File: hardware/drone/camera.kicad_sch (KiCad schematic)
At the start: 15 parts, among them J1 54548-2272, U1 STM32N645I0, U21 TCA9406DC, U25 ECMF2-40100N6, U26 ECMF2-40100N6, U27 ECMF2-40100N6

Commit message: Started footprint assignments
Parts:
- D6, D7, D8, D9: footprint Package_DIP:DIP-40_W15.24mm -> (none)
- U25, U26, U27: footprint Package_DFN_QFN:ST_UQFN-6L_1.5x1.7mm_P0.5mm -> (none)
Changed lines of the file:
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@@
 			)
 		)
-		(property "Footprint" "Package_DFN_QFN:ST_UQFN-6L_1.5x1.7mm_P0.5mm"
+		(property "Footprint" ""
 			(at 146.05 27.94 0)
 			(hide yes)
@@
 			)
 		)
-		(property "Footprint" "Package_DFN_QFN:ST_UQFN-6L_1.5x1.7mm_P0.5mm"
+		(property "Footprint" ""
 			(at 146.05 44.45 0)
 			(hide yes)
@@
 			)
 		)
-		(property "Footprint" "Package_DIP:DIP-40_W15.24mm"
+		(property "Footprint" ""
 			(at 234.95 121.92 0)
 			(hide yes)
@@
 			)
 		)
-		(property "Footprint" "Package_DFN_QFN:ST_UQFN-6L_1.5x1.7mm_P0.5mm"
+		(property "Footprint" ""
 			(at 146.05 60.96 0)
 			(hide yes)
@@
 			)
 		)
-		(property "Footprint" "Package_DIP:DIP-40_W15.24mm"
+		(property "Footprint" ""
 			(at 207.01 121.92 0)
 			(hide yes)
@@
 			)
 		)
-		(property "Footprint" "Package_DIP:DIP-40_W15.24mm"
+		(property "Footprint" ""
 			(at 220.98 121.92 0)
 			(hide yes)
@@
 			)
 		)
-		(property "Footprint" "Package_DIP:DIP-40_W15.24mm"
+		(property "Footprint" ""
 			(at 248.92 121.92 0)
 			(hide yes)

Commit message: Continued footprint assignments
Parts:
- U21: footprint (none) -> Package_SO:VSSOP-8_2.3x2mm_P0.5mm
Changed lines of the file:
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@@
 			)
 		)
-		(property "Footprint" ""
+		(property "Footprint" "Package_SO:VSSOP-8_2.3x2mm_P0.5mm"
 			(at 62.23 129.54 0)
 			(hide yes)

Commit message: More footprints
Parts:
- removed U25, U26, U27: ECMF2-40100N6, symbol SoftDrone:ECMF2-40100N6
- added U25, U26, U27: ECMF2-40A100N6, ECMF2-40A100N6:ECMF240A100N6, symbol SoftDrone:ECMF2-40A100N6
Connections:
- net CSI_CKN: now also U25.6 (D+_ic)
- net CSI_CKN_CON: now also U25.1 (D+_con)
- net CSI_CKP: now also U25.5 (D-_ic)
- net CSI_CKP_CON: now also U25.2 (D-_con)
- net CSI_D0N: now also U26.6 (D+_ic)
- net CSI_D0N_CON: now also U26.1 (D+_con)
- net CSI_D0P: now also U26.5 (D-_ic)
- net CSI_D0P_CON: now also U26.2 (D-_con)
- net CSI_D1N: now also U27.6 (D+_ic)
- net CSI_D1N_CON: now also U27.1 (D+_con)
- net CSI_D1P: now also U27.5 (D-_ic)
- net CSI_D1P_CON: now also U27.2 (D-_con)
- net GND: now also U25.3 (GND), U25.4 (GND), U26.3 (GND), U26.4 (GND), U27.3 (GND), U27.4 (GND)

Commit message: More footprints
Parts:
- C116, C117: footprint (none) -> Capacitor_SMD:C_0402_1005Metric
- D6, D7, D8, D9: footprint (none) -> SoftDroneLibrary:TPD1E1B04DPYR
- R34: footprint (none) -> Resistor_SMD:R_0402_1005Metric
- R41, R42: footprint (none) -> Resistor_SMD:R_0603_1608Metric
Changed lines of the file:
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@@
 			)
 		)
-		(property "Footprint" ""
+		(property "Footprint" "SoftDroneLibrary:TPD1E1B04DPYR"
 			(at 234.95 121.92 0)
 			(hide yes)
@@
 			)
 		)
-		(property "Footprint" ""
+		(property "Footprint" "Resistor_SMD:R_0603_1608Metric"
 			(at 150.622 114.3 90)
 			(hide yes)
@@
 			)
 		)
-		(property "Footprint" ""
+		(property "Footprint" "Resistor_SMD:R_0402_1005Metric"
 			(at 78.74 72.898 90)
 			(hide yes)
@@
 			)
 		)
-		(property "Footprint" ""
+		(property "Footprint" "SoftDroneLibrary:TPD1E1B04DPYR"
 			(at 207.01 121.92 0)
 			(hide yes)
@@
 			)
 		)
-		(property "Footprint" ""
+		(property "Footprint" "Capacitor_SMD:C_0402_1005Metric"
 			(at 85.3948 121.92 0)
 			(hide yes)
@@
 			)
 		)
-		(property "Footprint" ""
+		(property "Footprint" "Resistor_SMD:R_0603_1608Metric"
 			(at 141.732 114.3 90)
 			(hide yes)
@@
 			)
 		)
-		(property "Footprint" ""
+		(property "Footprint" "SoftDroneLibrary:TPD1E1B04DPYR"
 			(at 220.98 121.92 0)
 			(hide yes)
@@
 			)
 		)
-		(property "Footprint" ""
+		(property "Footprint" "Capacitor_SMD:C_0402_1005Metric"
 			(at 59.3852 121.92 0)
 			(hide yes)
@@
 			)
 		)
-		(property "Footprint" ""
+		(property "Footprint" "SoftDroneLibrary:TPD1E1B04DPYR"
 			(at 248.92 121.92 0)
 			(hide yes)

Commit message: Labeled nets, added colours, and fixed stm32n6 schematic symbol issues
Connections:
- net CSI_REXT: now reaches R34.1, U1.N5 (CSI_REXT)
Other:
- moved on the sheet: R34
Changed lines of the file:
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@@
+	(wire
+		(pts
+			(xy 71.12 71.12) (xy 78.74 71.12)
+		)
+		(stroke
+			(width 0)
+			(type default)
+		)
+	)
 	(wire
 		(pts
@@
 	(wire
 		(pts
-			(xy 86.36 71.12) (xy 86.36 73.66)
+			(xy 90.17 71.12) (xy 90.17 73.66)
 		)
 		(stroke
@@
 	(wire
 		(pts
-			(xy 82.55 71.12) (xy 86.36 71.12)
+			(xy 86.36 71.12) (xy 90.17 71.12)
 		)
 		(stroke
@@
 	(wire
 		(pts
-			(xy 71.12 71.12) (xy 74.93 71.12)
-		)
-		(stroke
-			(width 0)
-			(type default)
-		)
-	)
-	(wire
-		(pts
 			(xy 172.72 113.03) (xy 220.98 113.03)
 		)
@@
 			(width 0)
 			(type default)
+		)
+	)
+	(label "CSI_REXT"
+		(at 72.39 71.12 0)
+		(effects
+			(font
+				(size 0.762 0.762)
+				(thickness 0.254)
+				(bold yes)
+			)
+			(justify left bottom)
 		)
 	)
@@
 	(symbol
 		(lib_id "power:GND")
-		(at 86.36 73.66 0)
+		(at 90.17 73.66 0)
 		(mirror y)
 		(unit 1)
@@
 		(fields_autoplaced yes)
 		(property "Reference" "#PWR0190"
-			(at 86.36 80.01 0)
+			(at 90.17 80.01 0)
 			(hide yes)
 			(show_name no)
@@
 		)
 		(property "Value" "GND"
-			(at 86.36 78.74 0)
+			(at 90.17 78.74 0)
 			(show_name no)
 			(do_not_autoplace no)
@@
 		)
 		(property "Footprint" ""
-			(at 86.36 73.66 0)
+			(at 90.17 73.66 0)
 			(hide yes)
 			(show_name no)
@@
 		)
 		(property "Datasheet" ""
-			(at 86.36 73.66 0)
+			(at 90.17 73.66 0)
 			(hide yes)
 			(show_name no)
@@
 		)
 		(property "Description" "Power symbol creates a global label with name \"GND\" , ground"
-			(at 86.36 73.66 0)
+			(at 90.17 73.66 0)
 			(hide yes)
 			(show_name no)
@@
 	(symbol
 		(lib_id "Device:R")
-		(at 78.74 71.12 90)
+		(at 82.55 71.12 90)
 		(unit 1)
 		(body_style 1)
@@
 		(dnp no)
 		(property "Reference" "R34"
-			(at 78.74 68.58 90)
+			(at 82.55 68.58 90)
 			(show_name no)
 			(do_not_autoplace no)
@@
 		)
 		(property "Value" "200R"
-			(at 78.74 71.12 90)
+			(at 82.55 71.12 90)
 			(show_name no)
 			(do_not_autoplace no)
@@
 		)
 		(property "Footprint" "Resistor_SMD:R_0402_1005Metric"
-			(at 78.74 72.898 90)
+			(at 82.55 72.898 90)
 			(hide yes)
 			(show_name no)
@@
 		)
 		(property "Datasheet" ""
-			(at 78.74 71.12 0)
+			(at 82.55 71.12 0)
 			(hide yes)
 			(show_name no)
@@
 		)
 		(property "Description" "Resistor"
-			(at 78.74 71.12 0)
-			(hide yes)
-			(show_name no)
+			(at 82.55 71.12 0)
+			(hide yes)
+			(show_name no)

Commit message: Routed OSPI
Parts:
- U25, U26, U27: footprint ECMF2-40A100N6:ECMF240A100N6 -> SoftDroneLibrary:ECMF2-40A100N6
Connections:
- net CSI_CKN_CON renamed CSI_CON_CKN
- net CSI_CKP_CON renamed CSI_CON_CKP
- net CSI_D0N_CON renamed CSI_CON_D0N
- net CSI_D0P_CON renamed CSI_CON_D0P
- net CSI_D1N_CON renamed CSI_CON_D1N
- net CSI_D1P_CON renamed CSI_CON_D1P
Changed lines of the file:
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@@
 		)
 	)
-	(label "CSI_D1N_CON"
-		(at 215.9 43.18 0)
+	(label "CSI_CON_D0N"
+		(at 215.9 35.56 0)
 		(effects
 			(font
@@
 		)
 	)
-	(label "CSI_CKP_CON"
+	(label "CSI_CON_CKP"
 		(at 175.26 27.94 180)
 		(effects
@@
 		)
 	)
-	(label "CSI_CKN_CON"
-		(at 215.9 50.8 0)
+	(label "CSI_CON_D1N"
+		(at 215.9 43.18 0)
 		(effects
 			(font
@@
 		)
 	)
-	(label "CSI_CKP_CON"
-		(at 215.9 53.34 0)
+	(label "CSI_CON_D1P"
+		(at 175.26 60.96 180)
 		(effects
 			(font
@@
 				(bold yes)
 			)
-			(justify left bottom)
+			(justify right bottom)
 		)
 	)
-	(label "CSI_D1P_CON"
-		(at 215.9 45.72 0)
+	(label "I2C1_SCL_3V3"
+		(at 100.33 138.43 180)
 		(effects
 			(font
 				(size 1.27 1.27)
-				(thickness 0.254)
-				(bold yes)
 			)
-			(justify left bottom)
+			(justify right bottom)
 		)
 	)
-	(label "CSI_D1P_CON"
-		(at 175.26 60.96 180)
+	(label "CSI_CON_D0P"
+		(at 215.9 38.1 0)
 		(effects
 			(font
@@
 				(bold yes)
 			)
-			(justify right bottom)
+			(justify left bottom)
 		)
 	)
-	(label "I2C1_SCL_3V3"
-		(at 100.33 138.43 180)
+	(label "CSI_CON_D0P"
+		(at 175.26 44.45 180)
 		(effects
 			(font
 				(size 1.27 1.27)
+				(thickness 0.254)
+				(bold yes)
 			)
 			(justify right bottom)
 		)
 	)
-	(label "CSI_D0P_CON"
-		(at 175.26 44.45 180)
+	(label "CSI_CON_D1N"
+		(at 175.26 58.42 180)
 		(effects
 			(font
@@
 		)
 	)
-	(label "CSI_D1N_CON"
-		(at 175.26 58.42 180)
+	(label "CSI_CKP"
+		(at 119.38 27.94 0)
 		(effects
 			(font
@@
 				(bold yes)
 			)
-			(justify right bottom)
+			(justify left bottom)
 		)
 	)
-	(label "CSI_CKP"
-		(at 119.38 27.94 0)
+	(label "CSI_CON_CKP"
+		(at 215.9 53.34 0)
 		(effects
 			(font
@@
 		)
 	)
-	(label "CSI_D0N_CON"
+	(label "CSI_CON_D0N"
 		(at 175.26 41.91 180)
 		(effects
@@
 		)
 	)
-	(label "CSI_CKN_CON"
+	(label "CSI_CON_CKN"
 		(at 175.26 25.4 180)
 		(effects
@@
 		)
 	)
-	(label "CSI_D0N_CON"
-		(at 215.9 35.56 0)
+	(label "I2C1_SDA_3V3"
+		(at 217.17 83.82 0)
 		(effects
 			(font
 				(size 1.27 1.27)
-				(thickness 0.254)
-				(bold yes)
 			)
 			(justify left bottom)
 		)
 	)
-	(label "I2C1_SDA_3V3"
-		(at 217.17 83.82 0)
+	(label "CSI_CON_D1P"
+		(at 215.9 45.72 0)
 		(effects
 			(font
 				(size 1.27 1.27)
+				(thickness 0.254)
+				(bold yes)
 			)
 			(justify left bottom)
@@
 		)
 	)
-	(label "CSI_D0P_CON"
-		(at 215.9 38.1 0)
+	(label "CSI_CON_CKN"
+		(at 215.9 50.8 0)
 		(effects
 			(font
@@
 			)
 		)
-		(property "Footprint" "ECMF2-40A100N6:ECMF240A100N6"
+		(property "Footprint" "SoftDroneLibrary:ECMF2-40A100N6"
 			(at 146.05 60.96 0)
 			(hide yes)
@@
 			)
 		)
-		(property "Footprint" "ECMF2-40A100N6:ECMF240A100N6"
+		(property "Footprint" "SoftDroneLibrary:ECMF2-40A100N6"
 			(at 146.05 27.94 0)
 			(hide yes)
@@
 			)
 		)
-		(property "Footprint" "ECMF2-40A100N6:ECMF240A100N6"
+		(property "Footprint" "SoftDroneLibrary:ECMF2-40A100N6"
 			(at 146.05 44.45 0)
 			(hide yes)

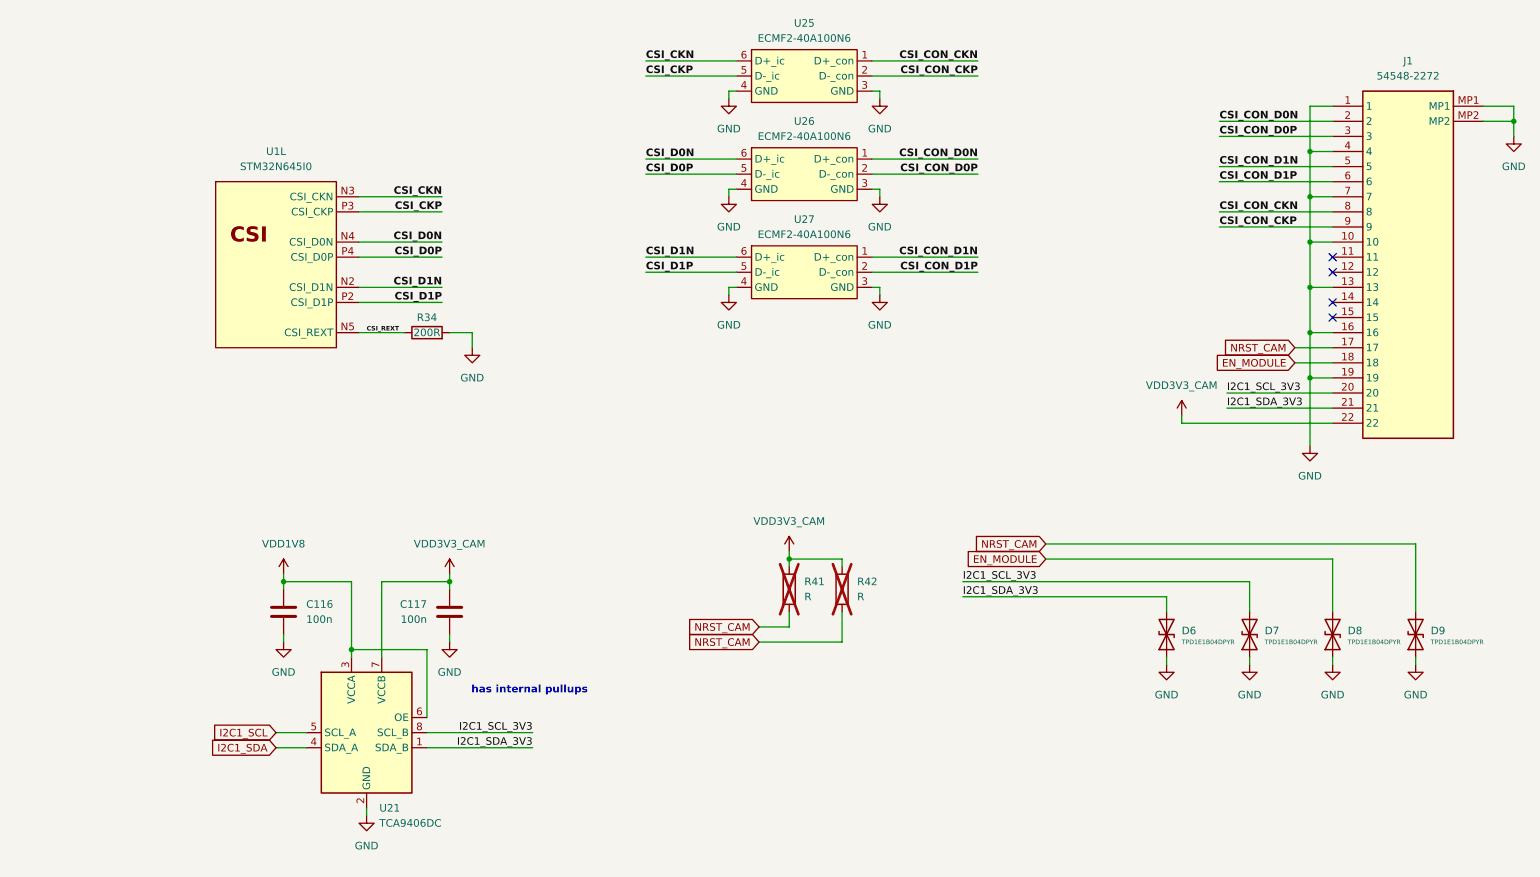
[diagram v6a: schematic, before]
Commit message: Schematic cleanup and changed pi network footprints
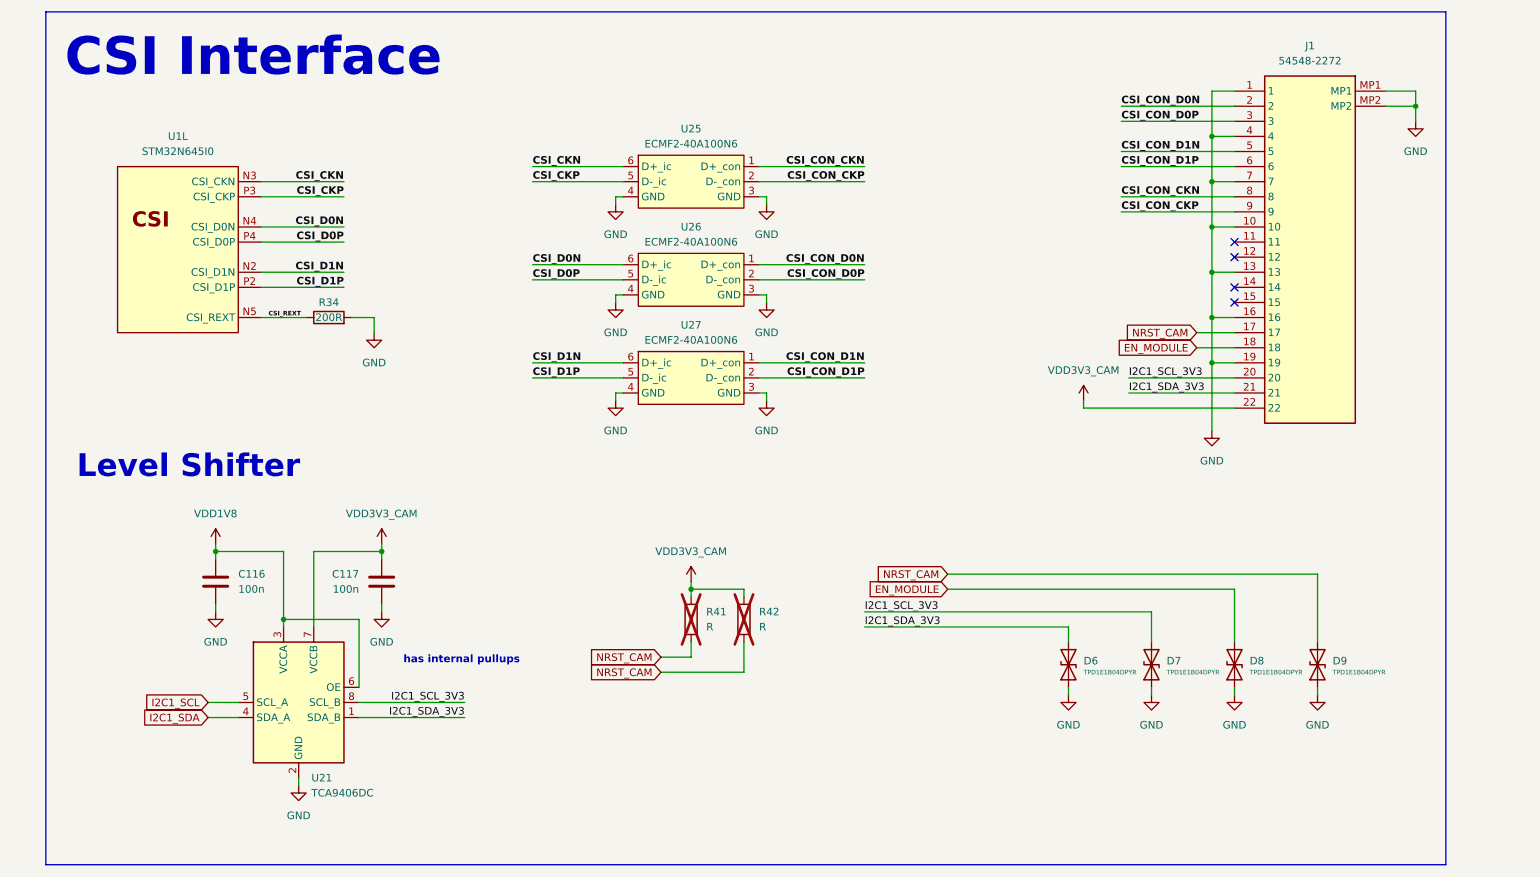
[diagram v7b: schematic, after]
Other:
- note added: "CSI Interface"
- note added: "Level Shifter"
- moved on the sheet: C116, C117, D6, D7, D8, D9, J1, R34, R41, R42, U1L, U21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
